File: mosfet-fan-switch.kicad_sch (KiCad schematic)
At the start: 35 parts, among them J1 12V IN, J3 FAN OUT, J4 NUC FAN HEADER, J5 FTDI HEADER, J6 ICSP, Q1 irfz44n, Q2 2n7002, Q3 irf7416, Q4 BC547, U1 Arduino_Pro_Mini_3V3

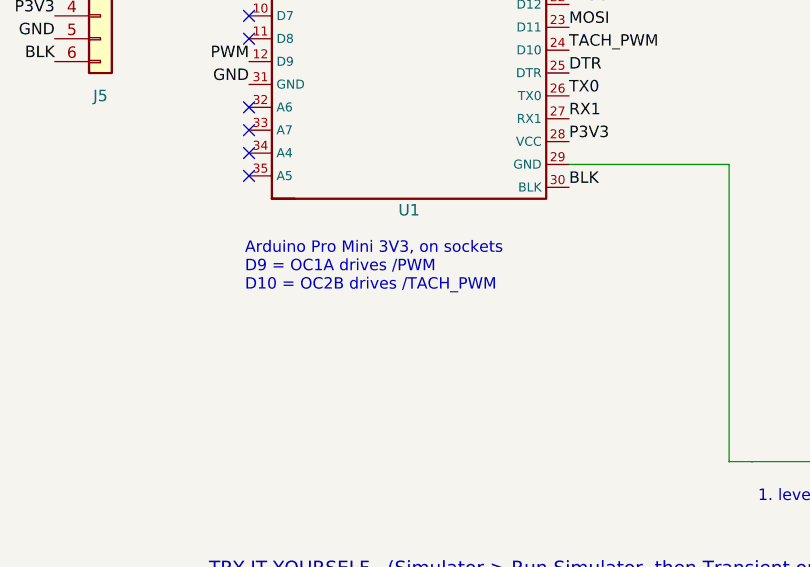
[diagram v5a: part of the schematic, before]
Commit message: docs: rewrite the board notes and README around the embedded module
docs/pcb-notes.md is the build sheet, so it now carries what the board actually
is: 56 x 92 mm, 30 footprints, the module deck, the full 35-hole U1 pad -> net
table, J5 and J6, the two spare diode footprints, and the 102-hole drill set
(0.8 x29, 1.0 x59, 1.1 x8, 1.2 x2, 3.2 x4 - verified against the Excellon file).

  * The corridor plan is spelled out net by net, because the two full-width
    rails are walls and the left edge holds four lanes in six mm.
  * "/P12V -> U1 pad 13" is named as the one connection the generator will not
    draw, with three honest ways to finish it and the recommendation (re-home
    the module's GND feed and the jumper becomes unnecessary).
  * Programming the module: J5 pin-for-pin with the BLK end marked, the 3.3 V
    adapter requirement, the five-wire Uno-as-ISP rule and why J6 pin 2 is a
    dead pad, the IDE's "ATmega328P (3.3V, 8MHz)" setting, and measuring your
    board's row spacing before soldering sockets.
  * The fan ladder now names D2 and D3 instead of a hypothetical part.
  * KiCad 10 findings added: the lib_symbols cache is the only thing kicad-cli
    resolves, a .kicad_sch wire is exactly two points, ERC's connection grid is
    1.27 mm, and kicad-cli needs the project tables beside the sheet.

README gets the same numbers, the new tools in the file tree, the
stale-until-routed warning, and a "Programming the module" section. The
schematic's own note is fixed: D10 is OC1B (Timer 1 channel B), not OC2B -
both this board's pins are on the same timer.

Every plotted output regenerated from the skeleton: etch SVG/PDF (page is
55.98 x 92.00 mm), both assembly PDFs, three renders, Gerbers and the drill
file plus map. Schematic re-exported. ERC 0/0, DRC 7 cosmetic + 68 expected.
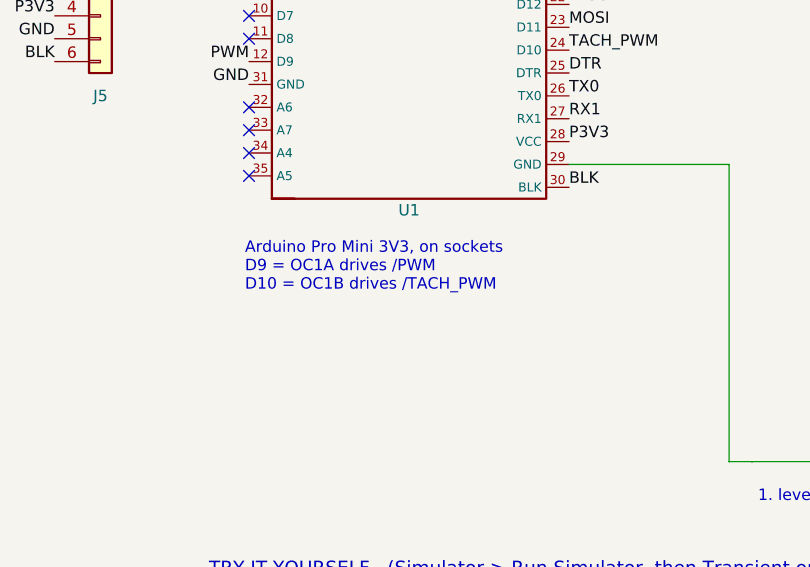
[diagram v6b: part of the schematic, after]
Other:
- note added: "Arduino Pro Mini 3V3, on sockets D9 = OC1A drives /PWM D10 = OC1B drives /TACH_PWM"
- note removed: "Arduino Pro Mini 3V3, on sockets D9 = OC1A drives /PWM D10 = OC2B drives /TACH_PWM"
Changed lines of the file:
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@@
 		)
 	)
-	(text "Arduino Pro Mini 3V3, on sockets\nD9 = OC1A drives /PWM\nD10 = OC2B drives /TACH_PWM"
+	(text "Arduino Pro Mini 3V3, on sockets\nD9 = OC1A drives /PWM\nD10 = OC1B drives /TACH_PWM"
 		(exclude_from_sim no)
 		(at 44 192 0)
